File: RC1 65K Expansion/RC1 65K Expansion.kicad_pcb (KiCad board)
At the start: 2 copper layers, 99.1 x 45.7 mm, 20 parts, among them J1 Expansion, J2 External IO, J3 Extra, U1 74LS138, U2 74LS145, U3 74LS08, U4 R6532

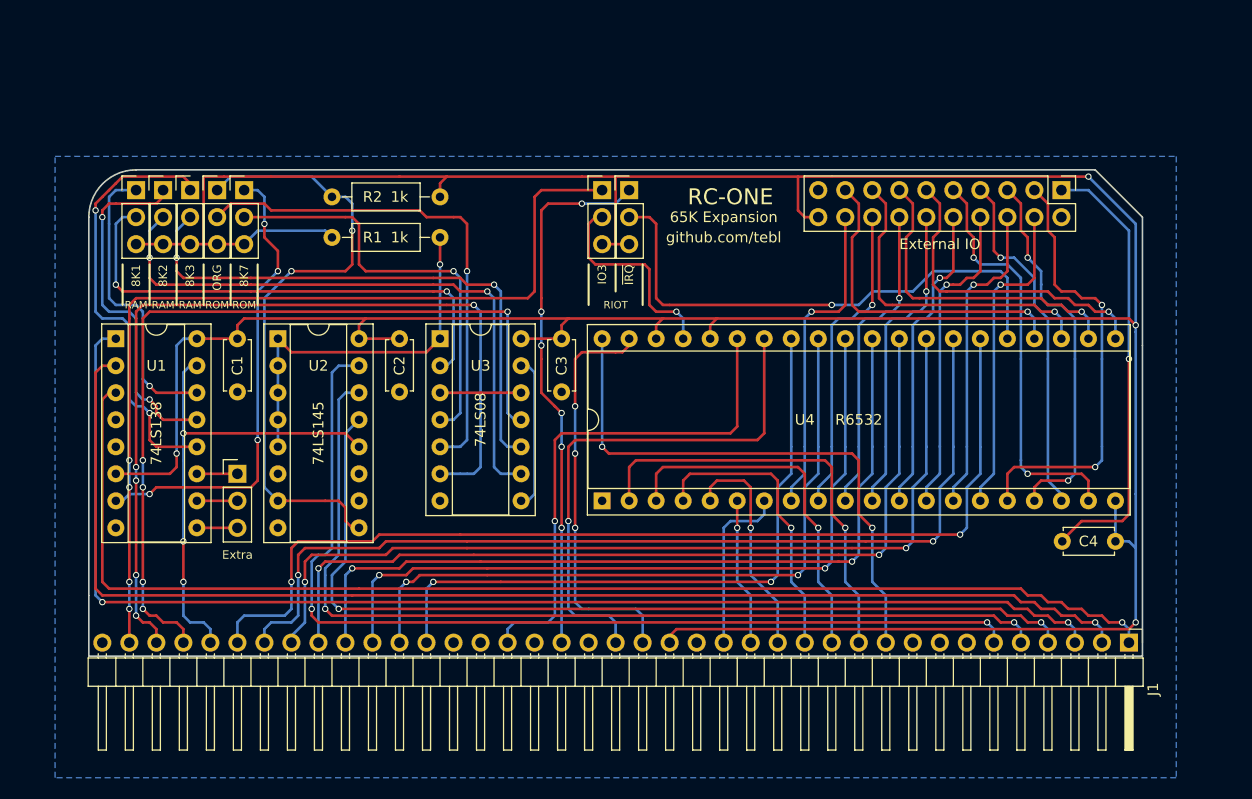
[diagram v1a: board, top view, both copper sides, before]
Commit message: 65K layout updated
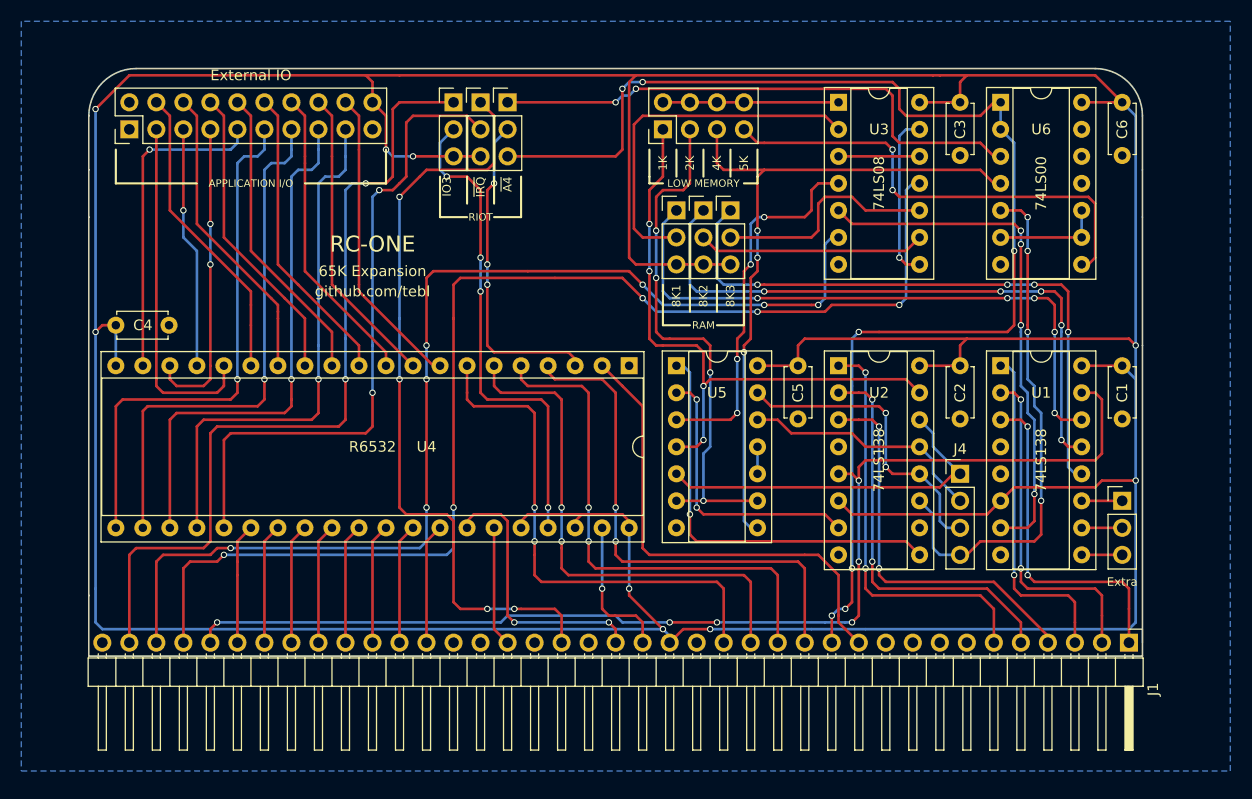
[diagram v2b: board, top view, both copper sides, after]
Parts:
- removed JP7: 8K7_ROM, Pin_Headers:Pin_Header_Straight_1x03_Pitch2.54mm
- removed R1, R2: 1k, Resistors_THT:R_Axial_DIN0207_L6.3mm_D2.5mm_P10.16mm_Horizontal
- added C5: 100nF, Capacitors_THT:C_Disc_D4.7mm_W2.5mm_P5.00mm, F.Cu at (158.1, 112.4)
- added C6: 100nF, Capacitors_THT:C_Disc_D4.7mm_W2.5mm_P5.00mm, F.Cu at (188.6, 87.6)
- added J4: K1-K4, Pin_Headers:Pin_Header_Straight_1x04_Pitch2.54mm, F.Cu at (173.4, 122.6)
- added J5: LOW RAM, Pin_Headers:Pin_Header_Straight_2x04_Pitch2.54mm, F.Cu at (145.4, 90.2)
- added U5: 74LS08, Housings_DIP:DIP-14_W7.62mm_Socket, F.Cu at (146.7, 112.4)
- added U6: 74LS00, Housings_DIP:DIP-14_W7.62mm_Socket, F.Cu at (177.2, 87.6)
- JP3: value ORG_ROM -> A4_INV
- U2: value 74LS145 -> 74LS138
- moved C4 96.2 mm to (94.0, 108.6), turned to 0 degrees
- moved J2 87.8 mm to (95.2, 90.2), turned to 90 degrees
- moved C1 83.2 mm to (188.6, 112.4)
- moved J3 83.2 mm to (188.6, 125.1)
- moved U1 83.2 mm to (177.2, 112.4)
- moved U2 52.8 mm to (161.9, 112.4)
- moved C2 52.8 mm to (173.4, 112.4)
- moved JP1 50.8 mm to (146.7, 97.8)
- moved JP2 50.8 mm to (149.2, 97.8)
- moved JP4 50.8 mm to (151.8, 97.8)
- moved U3 43.6 mm to (161.9, 87.6)
- moved C3 43.6 mm to (173.4, 87.6)
- moved JP3 28.5 mm to (130.8, 87.6)
- moved JP5 16.2 mm to (128.3, 87.6)
- moved JP6 16.2 mm to (125.7, 87.6)
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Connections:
- J1 pad 10: /A6 -> (no net)
- JP3 pad 1: ORG_ROM -> Net-(JP3-Pad1)
- JP3 pad 3: VCC -> /A4
- U2 pad 1: ORG_RAM -> /A10
- U2 pad 11: (no net) -> /K4
- U2 pad 12: DEN -> /K3
- U2 pad 13: /A12 -> /K2
- U2 pad 14: /A11 -> /K1
- U2 pad 15: /A10 -> /K0
- U2 pad 2: ORG_RAM -> /A11
- U2 pad 3: ORG_RAM -> /A12
- U2 pad 4: ORG_RAM -> GND
- U2 pad 5: ORG_RAM -> DEN
- U2 pad 6: (no net) -> VCC
- U2 pad 7: ORG_ROM -> /K7
- U2 pad 9: ORG_ROM -> /K6
- U3 pad 1: ORG_RAM -> ~LOW_RAM
- U3 pad 5: Net-(JP3-Pad2) -> /8K7
- U4 pad 3: /A4 -> Net-(JP3-Pad2)
- U4 pad 40: /A6 -> VCC
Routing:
- net VCC: track 347.7 -> 461.8 mm, vias 4 -> 9
- net /A4: track 34.0 -> 122.5 mm, vias 1 -> 7
- net /A13: track 120.3 -> 31.9 mm, vias 2 -> 1
- net /A14: track 120.0 -> 31.9 mm, vias 1 -> 2
- net /A15: track 118.3 -> 31.9 mm, vias 1 -> 2
- net /D7: track 95.8 -> 11.3 mm, vias 2 -> 0
- net /D6: track 90.7 -> 11.3 mm, vias 2 -> 0
- net /D5: track 85.7 -> 11.3 mm, vias 2 -> 0
- net /D4: track 81.3 -> 11.3 mm, vias 2 -> 0
- net /RAM_4K: track 0.00 -> 66.0 mm, vias 0 -> 3
- net DEN: track 45.8 -> 110.7 mm, vias 3 -> 6
- net /D3: track 76.2 -> 11.3 mm, vias 2 -> 0
- net /D2: track 71.2 -> 11.3 mm, vias 2 -> 0
- net /K0: track 0.00 -> 58.6 mm, vias 0 -> 4
- net ORG_ROM: track 58.6 -> 0.00 mm, vias 2 -> 0
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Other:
- board size 99.1 x 45.7 mm -> 99.1 x 55.2 mm
- board text added: "1K"
- board text added: "2K"
- board text added: "4K"
- board text added: "5K"
- board text added: "A4"
- board text added: "APPLICATION I/O"
- board text added: "INVERT"
- board text added: "LOW MEMORY"
- board text added: "Revision B"
- board text added: "~A4"
- board text removed: "$1800-"
- board text removed: "$1FFF"
- board text removed: "$E000-"
- board text removed: "$FFFF"
- board text removed: "8K DECODE"
- board text removed: "8K4"
- board text removed: "8K5"
- board text removed: "8K6"
- board text removed: "8K7"
- board text removed: "IO3 CS"
- board text removed: "LOGIC"
- board text removed: "ORG"
- board text removed: "ROM"
- board text removed: "Revision A"

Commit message: Gerber export
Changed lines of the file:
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@@
     (links 131)
     (no_connects 0)
-    (area 91.364999 84.379999 190.575001 139.775001)
+    (area 85.09 75.278095 198.755001 150.495001)
     (thickness 1.6)
     (drawings 176)
@@
       (effects (font (size 1 1) (thickness 0.15)))
     )
-    (fp_text value 74LS08 (at 3.81 17.57) (layer F.Fab)
-      (effects (font (size 1 1) (thickness 0.15)))
-    )
+    (fp_text value 74LS08 (at 3.81 7.62 90) (layer F.SilkS)
+      (effects (font (size 1 1) (thickness 0.15)))
+    )
